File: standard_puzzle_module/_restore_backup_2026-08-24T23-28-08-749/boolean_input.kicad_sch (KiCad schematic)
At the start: 6 parts

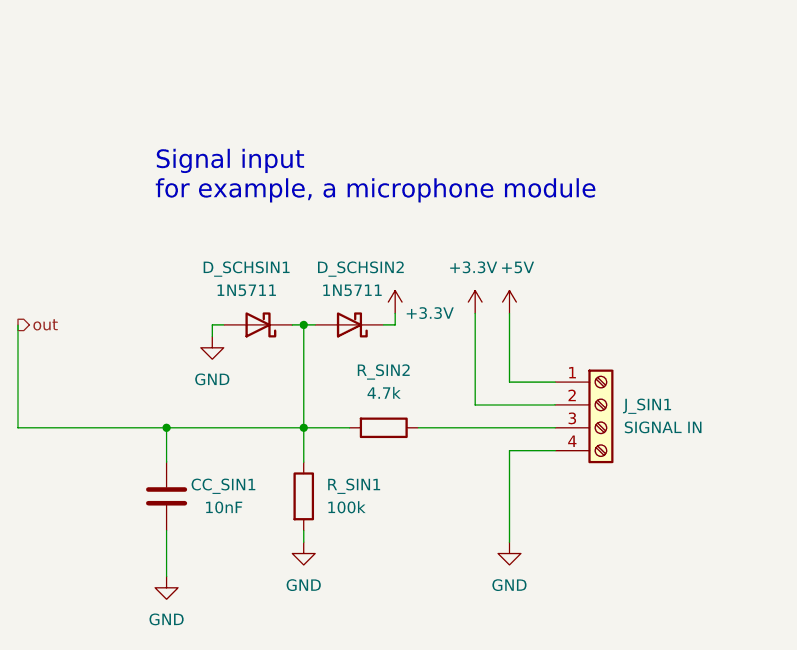
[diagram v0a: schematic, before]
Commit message: feat: draft component placement for pcb
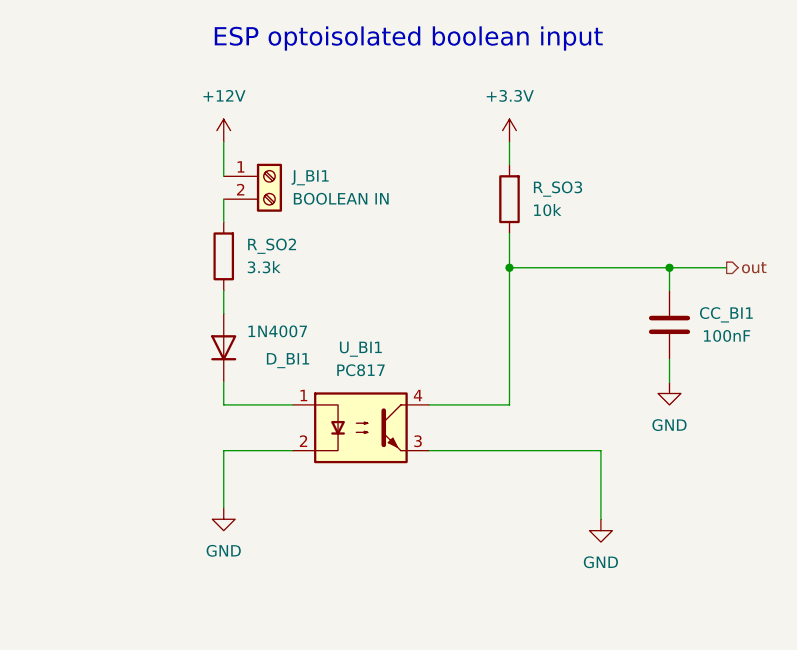
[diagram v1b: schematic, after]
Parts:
- removed CC_SIN1: 10nF, Capacitor_THT:C_Disc_D5.0mm_W2.5mm_P5.00mm, symbol Device:C
- removed D_SCHSIN1, D_SCHSIN2: 1N5711, Diode_THT:D_DO-35_SOD27_P7.62mm_Horizontal, symbol Diode:1N5711
- removed J_SIN1: SIGNAL IN, TerminalBlock_Phoenix:TerminalBlock_Phoenix_MKDS-1,5-4-5.08_1x04_P5.08mm_Horizontal, symbol Connector:Screw_Terminal_01x04
- removed R_SIN1: 100k, Resistor_THT:R_Axial_DIN0411_L9.9mm_D3.6mm_P15.24mm_Horizontal, symbol Device:R
- removed R_SIN2: 4.7k, Resistor_THT:R_Axial_DIN0411_L9.9mm_D3.6mm_P15.24mm_Horizontal, symbol Device:R
- added CC_BI1: 100nF, Capacitor_THT:C_Disc_D5.0mm_W2.5mm_P5.00mm, symbol Device:C
- added D_BI1: 1N4007, Diode_THT:D_DO-41_SOD81_P10.16mm_Horizontal, symbol Diode:1N4007
- added J_BI1: BOOLEAN IN, TerminalBlock_Phoenix:TerminalBlock_Phoenix_MKDS-1,5-2-5.08_1x02_P5.08mm_Horizontal, symbol Connector:Screw_Terminal_01x02
- added R_SO2: 3.3k, Resistor_THT:R_Axial_DIN0207_L6.3mm_D2.5mm_P10.16mm_Horizontal, symbol Device:R
- added R_SO3: 10k, Resistor_THT:R_Axial_DIN0207_L6.3mm_D2.5mm_P10.16mm_Horizontal, symbol Device:R
- added U_BI1: PC817, Package_DIP:DIP-4_W7.62mm, symbol Isolator:PC817
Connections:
- net +3.3V: now also R_SO3.2
- net GND: now also CC_BI1.2, U_BI1.2, U_BI1.3
- net out: now also CC_BI1.1, R_SO3.1, U_BI1.4
- new net: D_BI1.1 (K), U_BI1.1
- new net: D_BI1.2 (A), R_SO2.1
- new net: J_BI1.2 (Pin_2), R_SO2.2
- new net +12V: J_BI1.1 (Pin_1)
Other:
- note added: "ESP optoisolated boolean input"
- note removed: "Signal input for example, a microphone module"
- title: Signal input -> ESP optoisolated boolean input
